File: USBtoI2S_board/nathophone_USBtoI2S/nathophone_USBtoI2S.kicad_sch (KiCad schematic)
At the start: 18 parts, among them J1 Conn_01x30, J2 UJ20-C-H-G-SMT-5-P16-TR, J3 Conn_02x10_Odd_Even, Q1 MMBT3904, U1 IS25LP032D-JBLE

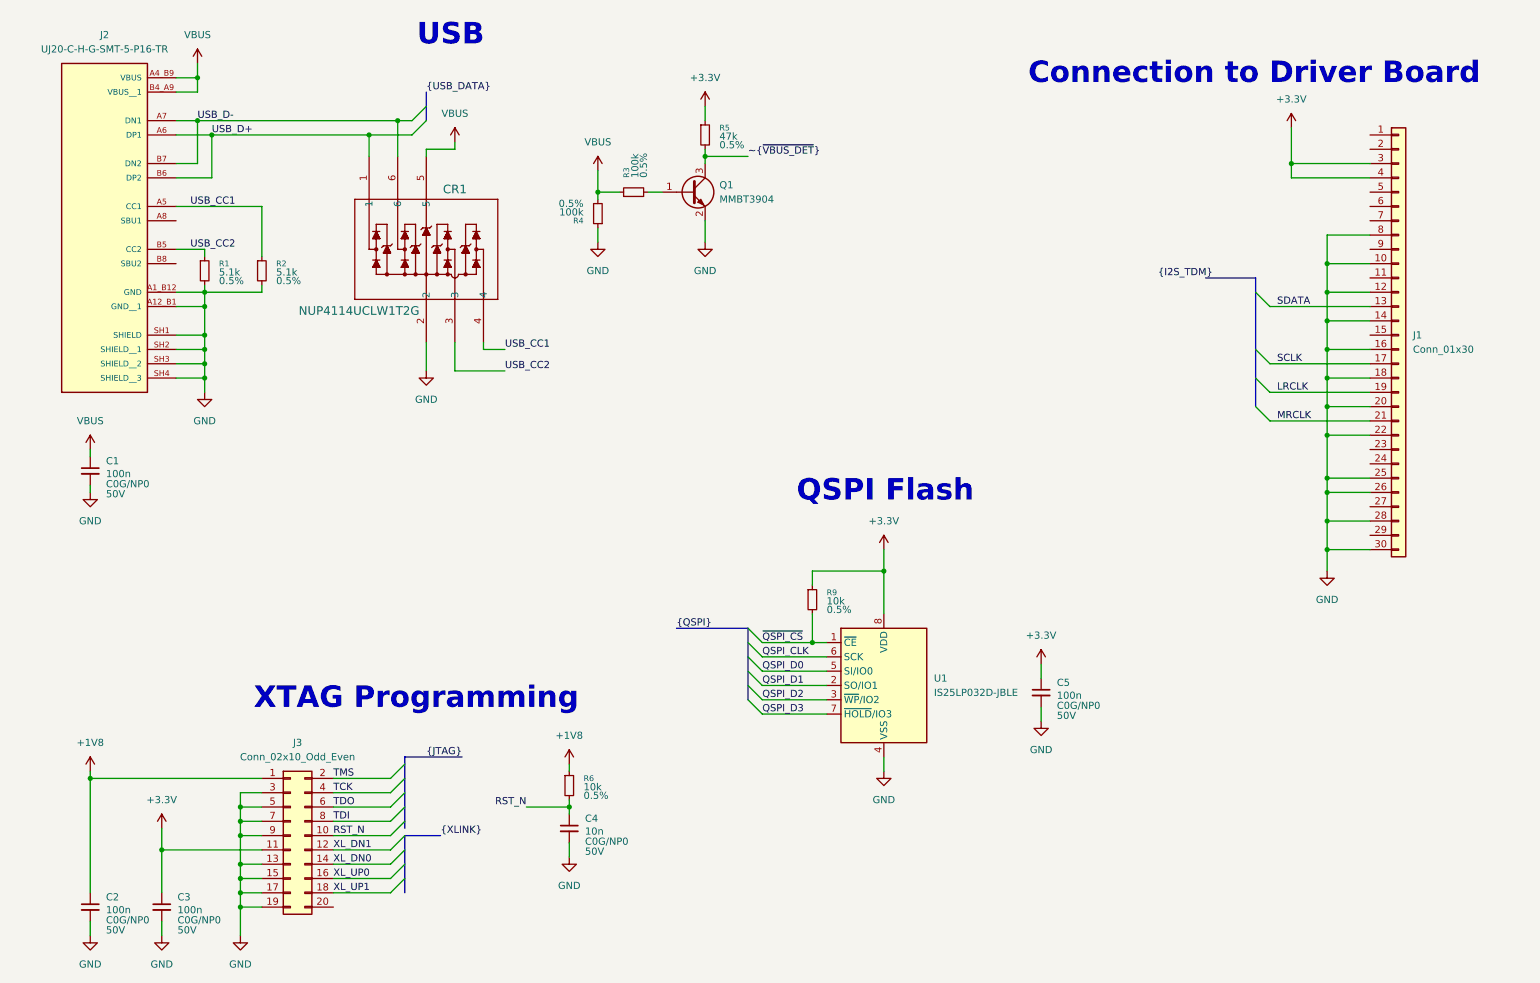
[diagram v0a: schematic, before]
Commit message: ADDED XMOS eval board design files, BEGUN layout of usbtoi2s board
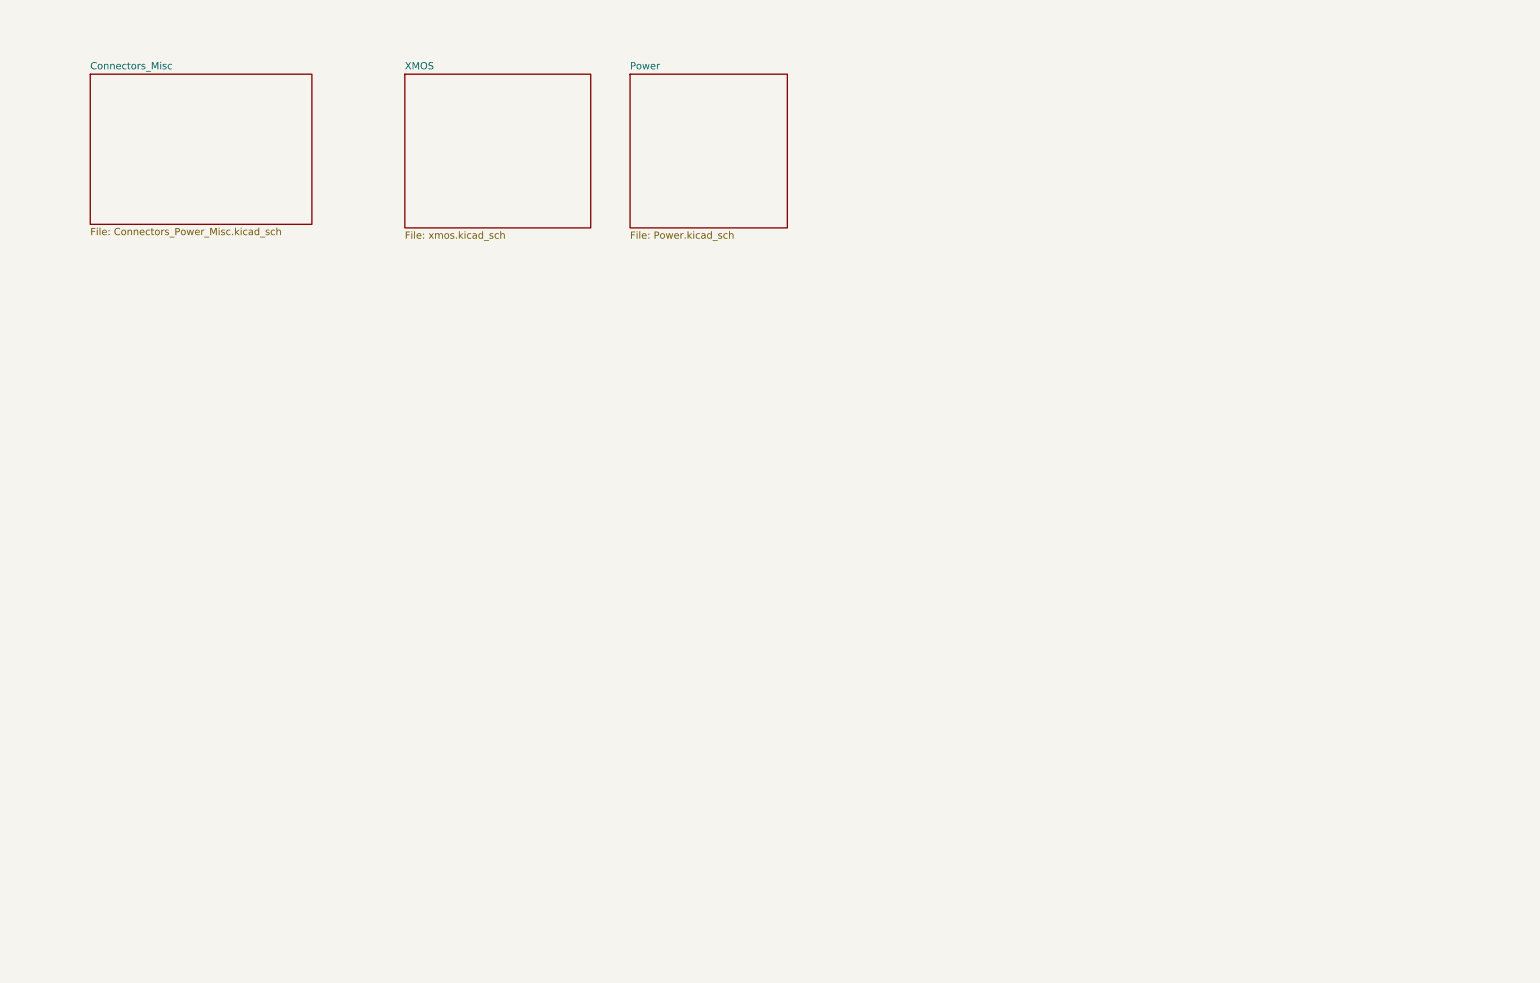
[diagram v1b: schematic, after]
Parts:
- removed C1, C2, C3, C5: 100n, USB_to_I2S_Board:CAPC1810X65N, symbol Device:C_Small
- removed C4: 10n, Capacitor_SMD:C_0805_2012Metric_Pad1.18x1.45mm_HandSolder, symbol Device:C_Small
- removed CR1: NUP4114UCLW1T2G, Package_TO_SOT_SMD:SOT-363_SC-70-6, symbol USB_to_I2S_Board:NUP4114UCLW1T2G
- removed J1: Conn_01x30, Nathophone_Driverboard:CON_525593072_MOL, symbol Connector_Generic:Conn_01x30
- removed J2: UJ20-C-H-G-SMT-5-P16-TR, USB_to_I2S_Board:SAMESKY_UJ20-C-H-G-SMT-5-P16-TR, symbol USB_to_I2S_Board:UJ20-C-H-G-SMT-5-P16-TR
- removed J3: Conn_02x10_Odd_Even, USB_to_I2S_Board:CON20_2X10_DUK_FTSH_SAI-M, symbol Connector_Generic:Conn_02x10_Odd_Even
- removed Q1: MMBT3904, Package_TO_SOT_SMD:SOT-23, symbol Transistor_BJT:MMBT3904
- removed R1, R2: 5.1k, Resistor_SMD:R_0805_2012Metric_Pad1.20x1.40mm_HandSolder, symbol Device:R_Small
- removed R3, R4: 100k, Resistor_SMD:R_0805_2012Metric_Pad1.20x1.40mm_HandSolder, symbol Device:R_Small
- removed R5: 47k, Resistor_SMD:R_0805_2012Metric_Pad1.20x1.40mm_HandSolder, symbol Device:R_Small
- removed R6, R9: 10k, Resistor_SMD:R_0805_2012Metric_Pad1.20x1.40mm_HandSolder, symbol Device:R_Small
- removed U1: IS25LP032D-JBLE, Package_SO:SOIC-8_5.3x5.3mm_P1.27mm, symbol Memory_Flash:SST25VF080B-50-4x-S2Ax
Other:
- added sheet Connectors_Misc (Connectors_Power_Misc.kicad_sch)
- added sheet Power (Power.kicad_sch)
- added sheet XMOS (xmos.kicad_sch)
- note removed: "Connection to Driver Board"
- note removed: "QSPI Flash"
- note removed: "USB"
- note removed: "XTAG Programming"
- company: Private -> (none)
- title: USB to I2S Module -> (none)
